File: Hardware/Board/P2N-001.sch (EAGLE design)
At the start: 35 parts, among them IC1 4053N, IC2 LTC485N, IC3 74LS07N, IC4 LTC485N, K1 G5V1, T1 2SC1815

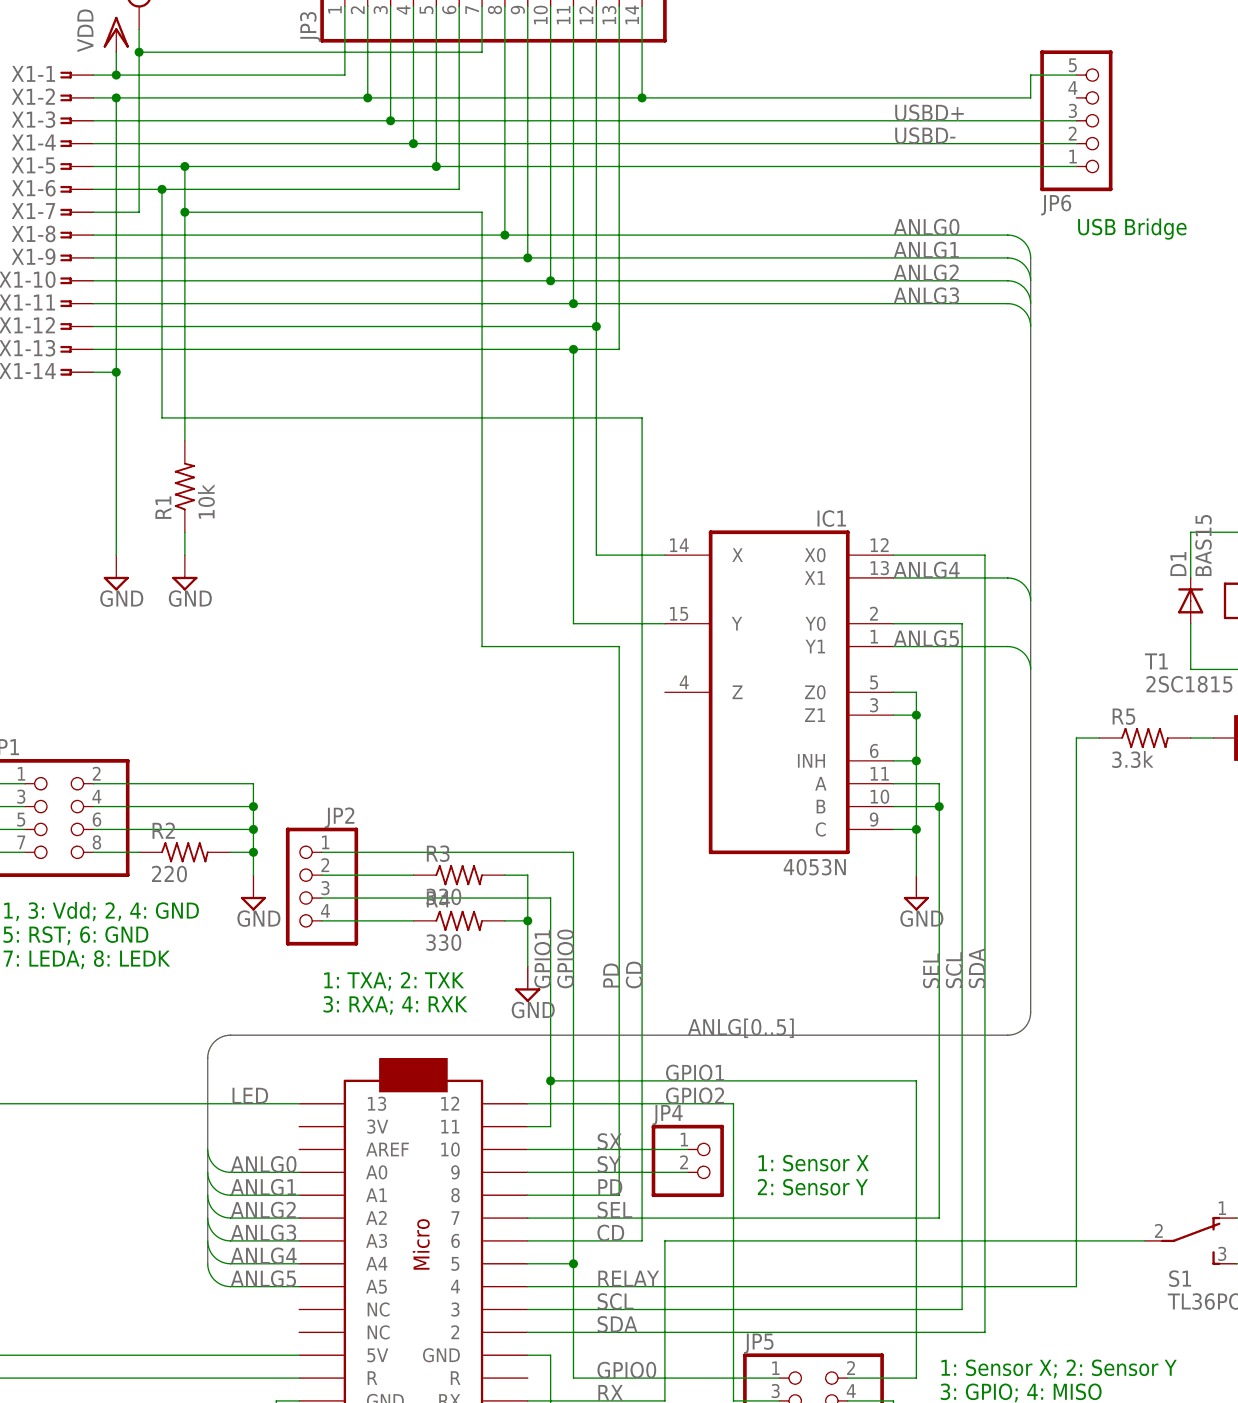
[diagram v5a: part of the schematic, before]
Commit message: Cleaned up schematic and board design of P2N.
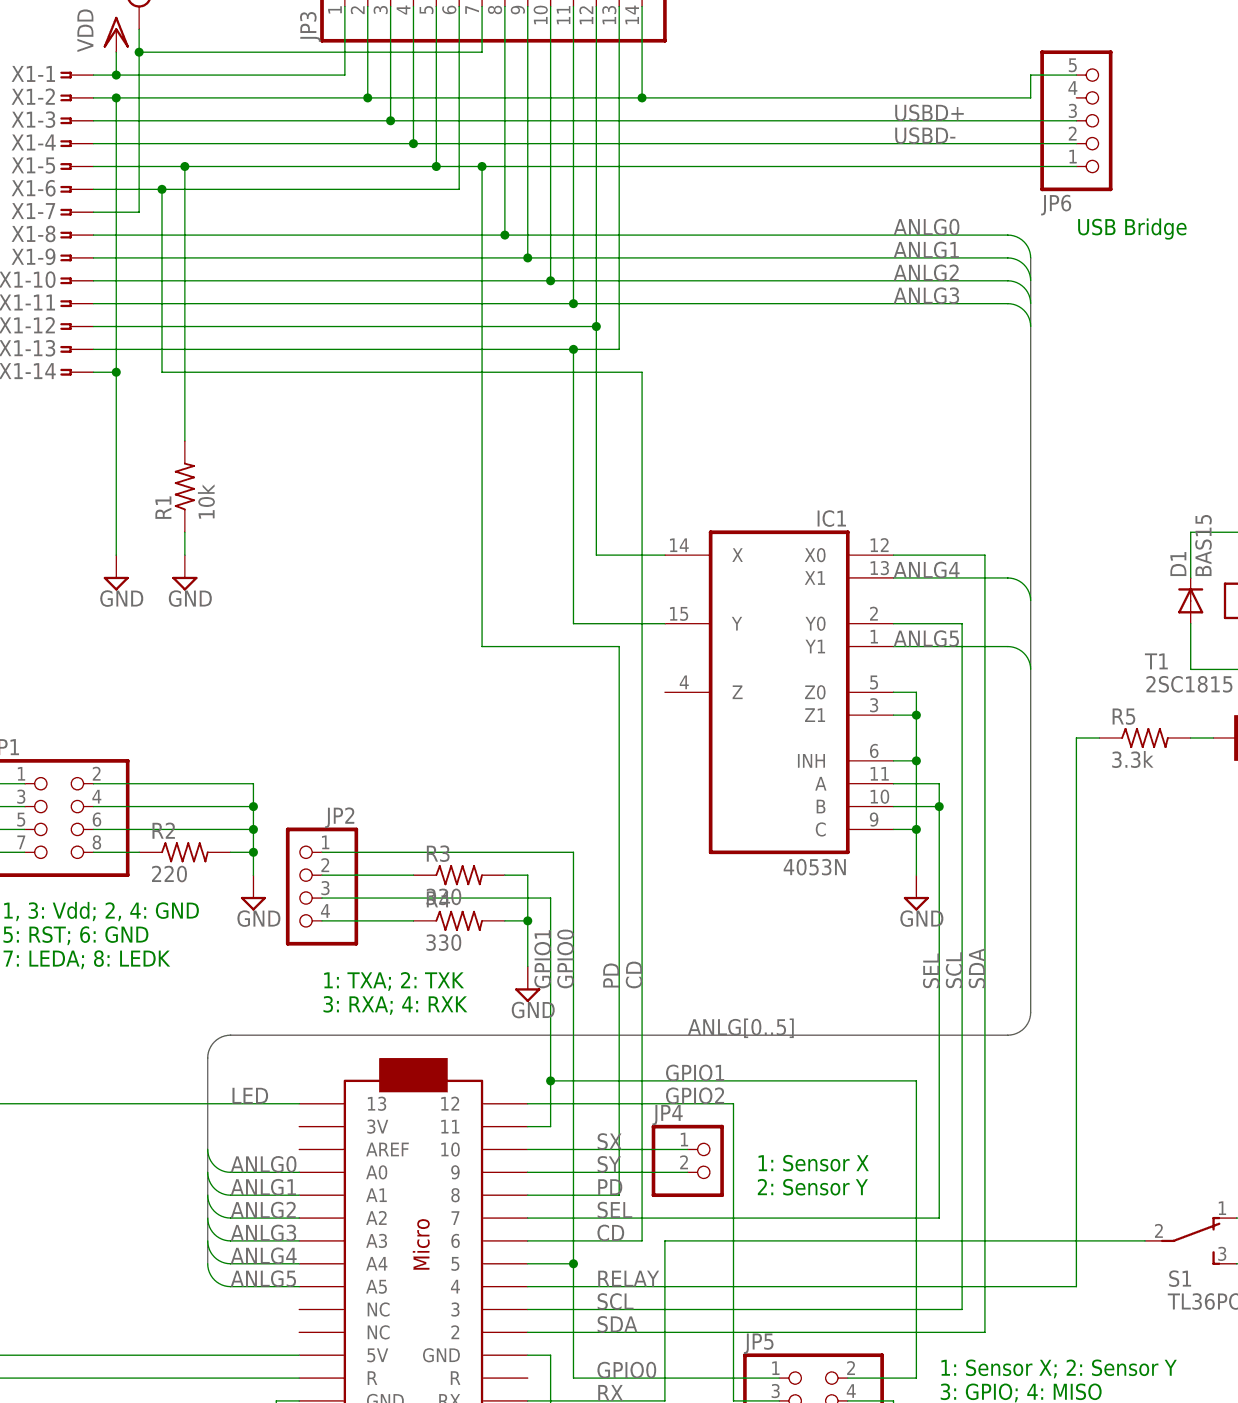
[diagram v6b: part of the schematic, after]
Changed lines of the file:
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@@
 <wire x1="22.86" y1="175.26" x2="33.02" y2="175.26" width="0.1524" layer="91"/>
 <wire x1="33.02" y1="175.26" x2="60.96" y2="175.26" width="0.1524" layer="91"/>
-<wire x1="60.96" y1="175.26" x2="132.08" y2="175.26" width="0.1524" layer="91"/>
-<wire x1="33.02" y1="175.26" x2="33.02" y2="170.18" width="0.1524" layer="91"/>
+<wire x1="60.96" y1="175.26" x2="66.04" y2="175.26" width="0.1524" layer="91"/>
 <pinref part="R1" gate="G$1" pin="2"/>
 <junction x="33.02" y="175.26"/>
-<wire x1="33.02" y1="170.18" x2="33.02" y2="144.78" width="0.1524" layer="91"/>
-<wire x1="33.02" y1="170.18" x2="66.04" y2="170.18" width="0.1524" layer="91"/>
-<junction x="33.02" y="170.18"/>
+<wire x1="66.04" y1="175.26" x2="132.08" y2="175.26" width="0.1524" layer="91"/>
+<wire x1="33.02" y1="175.26" x2="33.02" y2="144.78" width="0.1524" layer="91"/>
 <pinref part="JP3" gate="A" pin="5"/>
 <wire x1="60.96" y1="193.04" x2="60.96" y2="175.26" width="0.1524" layer="91"/>
 <junction x="60.96" y="175.26"/>
-<wire x1="66.04" y1="170.18" x2="66.04" y2="121.92" width="0.1524" layer="91"/>
+<pinref part="MC1" gate="G$1" pin="8"/>
+<wire x1="66.04" y1="175.26" x2="66.04" y2="121.92" width="0.1524" layer="91"/>
 <wire x1="66.04" y1="121.92" x2="81.28" y2="121.92" width="0.1524" layer="91"/>
 <wire x1="81.28" y1="121.92" x2="81.28" y2="60.96" width="0.1524" layer="91"/>
-<pinref part="MC1" gate="G$1" pin="8"/>
 <wire x1="81.28" y1="60.96" x2="71.12" y2="60.96" width="0.1524" layer="91"/>
 <label x="78.74" y="60.96" size="1.778" layer="95"/>
 <label x="81.28" y="83.82" size="1.778" layer="95" rot="R90"/>
+<junction x="66.04" y="175.26"/>
 </segment>
 </net>
@@
 <pinref part="X1" gate="-6" pin="1"/>
 <wire x1="22.86" y1="172.72" x2="30.48" y2="172.72" width="0.1524" layer="91"/>
-<wire x1="30.48" y1="172.72" x2="30.48" y2="147.32" width="0.1524" layer="91"/>
-<wire x1="30.48" y1="147.32" x2="83.82" y2="147.32" width="0.1524" layer="91"/>
+<wire x1="30.48" y1="172.72" x2="30.48" y2="152.4" width="0.1524" layer="91"/>
+<wire x1="30.48" y1="152.4" x2="83.82" y2="152.4" width="0.1524" layer="91"/>
 <pinref part="JP3" gate="A" pin="6"/>
 <wire x1="30.48" y1="172.72" x2="63.5" y2="172.72" width="0.1524" layer="91"/>
 <wire x1="63.5" y1="172.72" x2="63.5" y2="193.04" width="0.1524" layer="91"/>
 <junction x="30.48" y="172.72"/>
-<wire x1="83.82" y1="147.32" x2="83.82" y2="55.88" width="0.1524" layer="91"/>
+<wire x1="83.82" y1="152.4" x2="83.82" y2="55.88" width="0.1524" layer="91"/>
 <pinref part="MC1" gate="G$1" pin="6"/>
 <wire x1="83.82" y1="55.88" x2="71.12" y2="55.88" width="0.1524" layer="91"/>

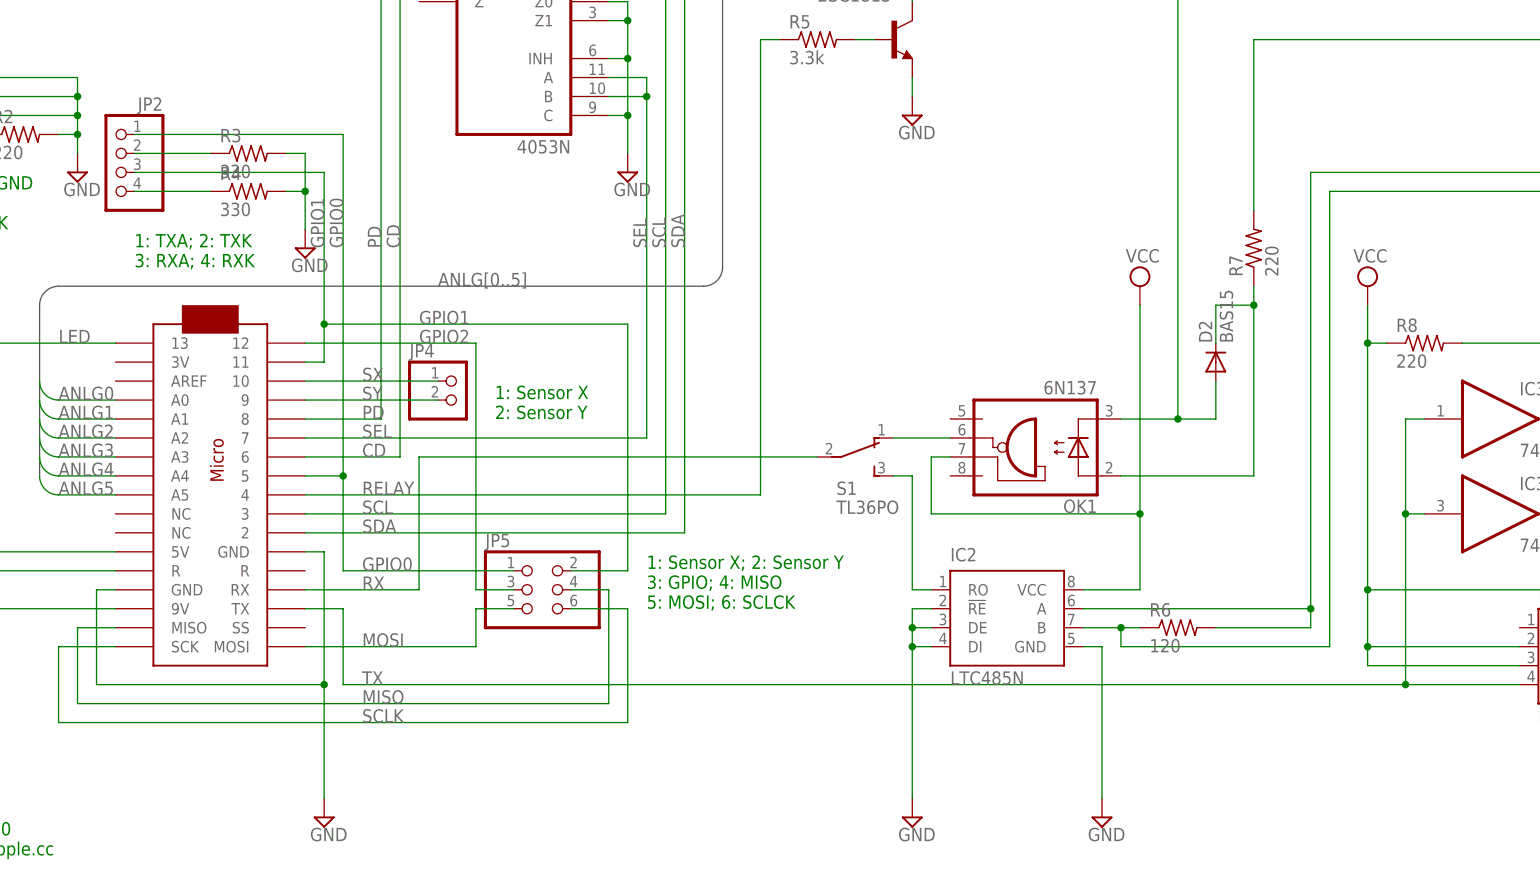
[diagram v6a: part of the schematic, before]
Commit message: Added Reset SW.
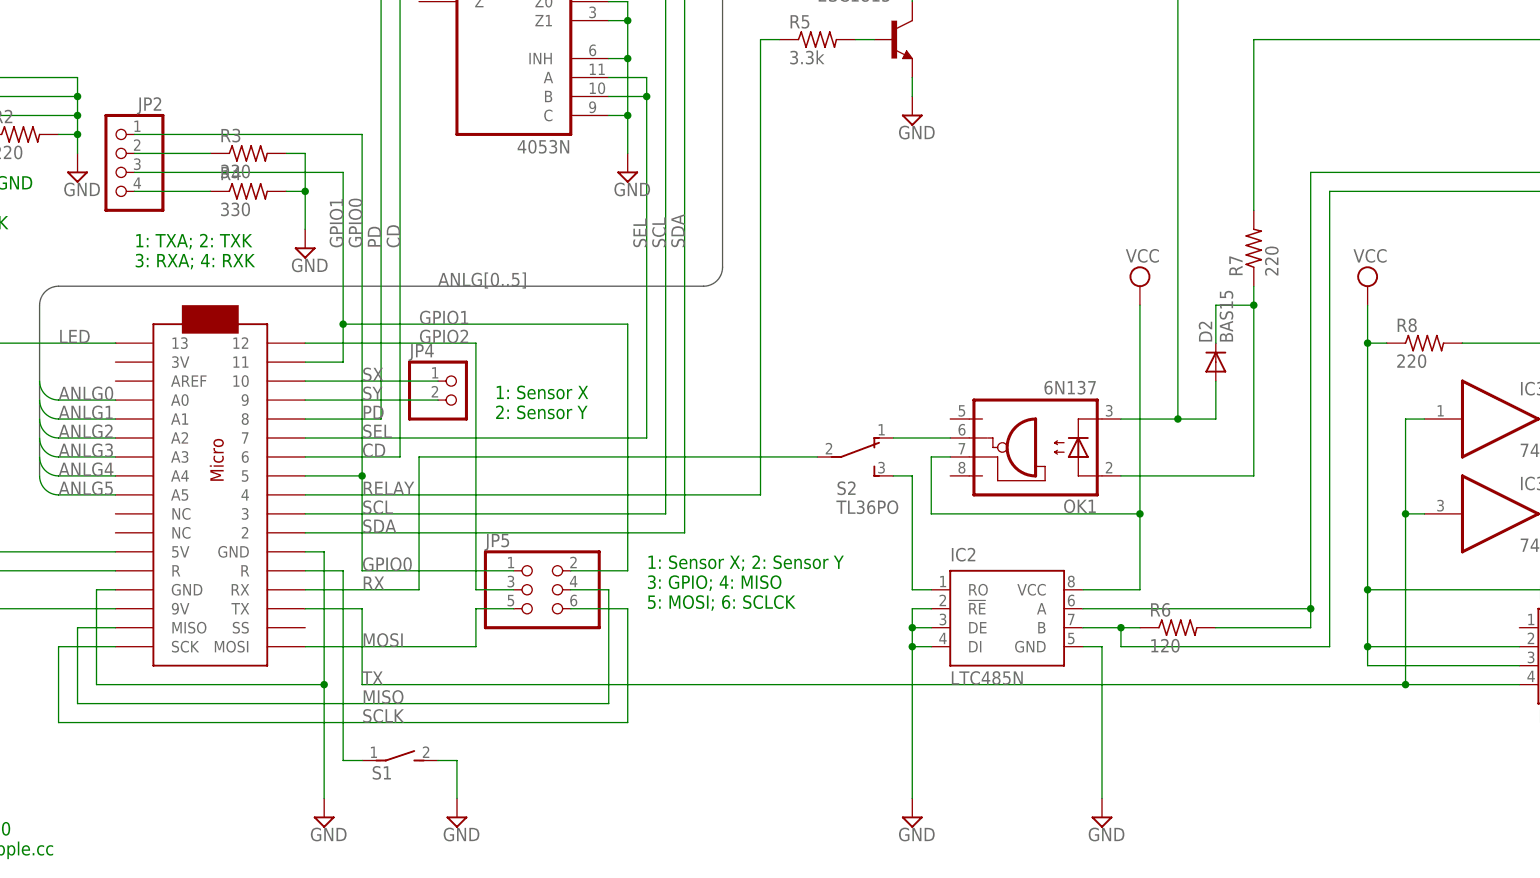
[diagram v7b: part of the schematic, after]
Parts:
- added S2: TL36PO, switch:TL36PO
- S1: value TL36PO -> (none); device switch:TL36PO -> switch-dil:DS01E
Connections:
- new net N$1: MC1.R@2, S1.1
- net GND: now also S1.2
- net MIDIRX: now also S2.O; no longer S1.O
- net RX: now also S2.P; no longer S1.P
- net XMIDIRX: now also S2.S; no longer S1.S
